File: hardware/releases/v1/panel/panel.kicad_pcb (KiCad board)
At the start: 4 copper layers, 126 x 56 mm, 125 parts, among them J1 12-32V DC In, J101 Main board, J102 XD_NORTH, J103 XD_EAST, J104 XD_SOUTH, J105 XD_WEST, J106 PIEZO_RAIN, J2 Crown board, J201 Probe T-Header SMD, J3 Probe board, J301 Main board, J302 Reflector T-Socket SMD, J4 SEN55 PM, Q1 AO3400A, Q301 AO3400A, SW1 SERVICE, U1 SCT2400TVBR, U101 SN74LVC2G04, U102 CD4052BM96, U103 TLV9062IDR, U104 LM393DR2G, U105 TLV9062IDR, U106 LTR-390UV-01, U107 VEML7700-TT, U108 LIS2MDLTR, U2 LM66100, U3 XIAO ESP32C6, U301 SCD41-D-R2, U302 SGP41-D-R4, U303 SHT45-AD1F-R2, U304 LM393DR2G, U4 BMP581, U5 LSM6DS3TR-C, U6 AS3935-BQFT, U7 74AHCT1G125

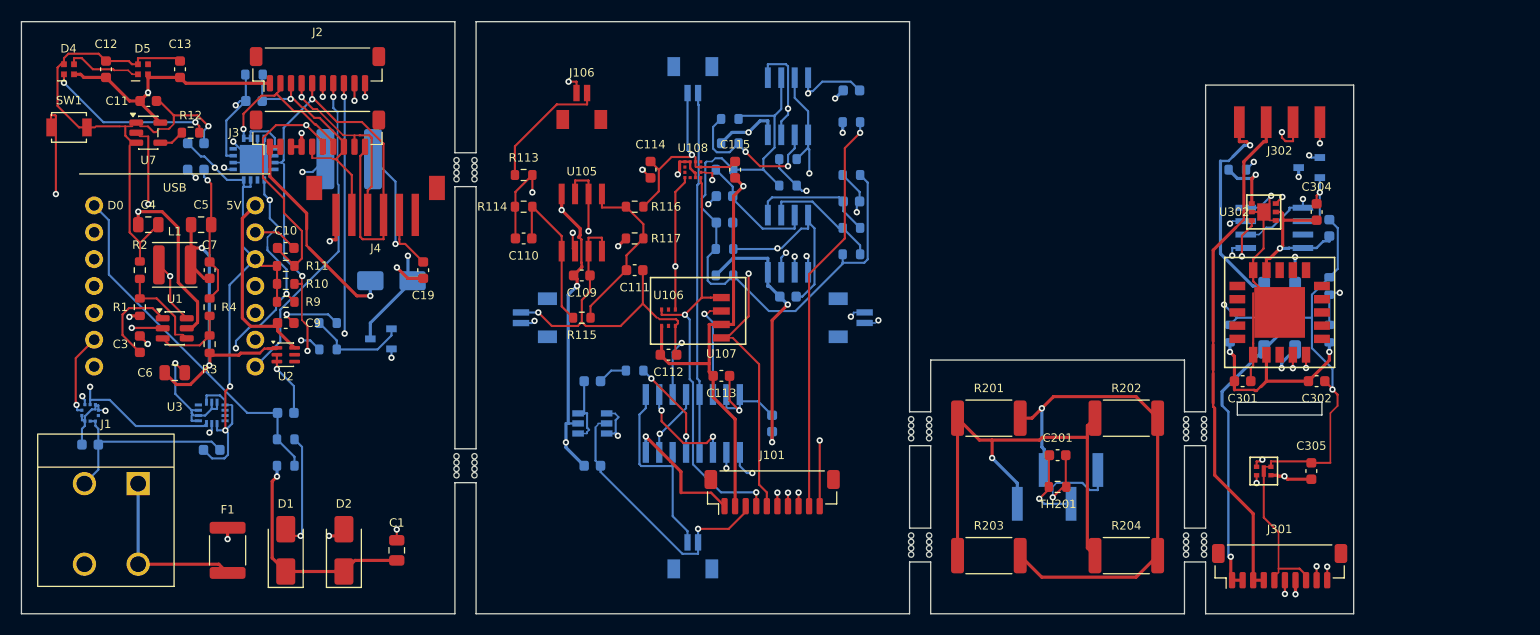
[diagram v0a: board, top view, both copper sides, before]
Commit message: Update project documentation and refactor crown sensor board circuit implementation
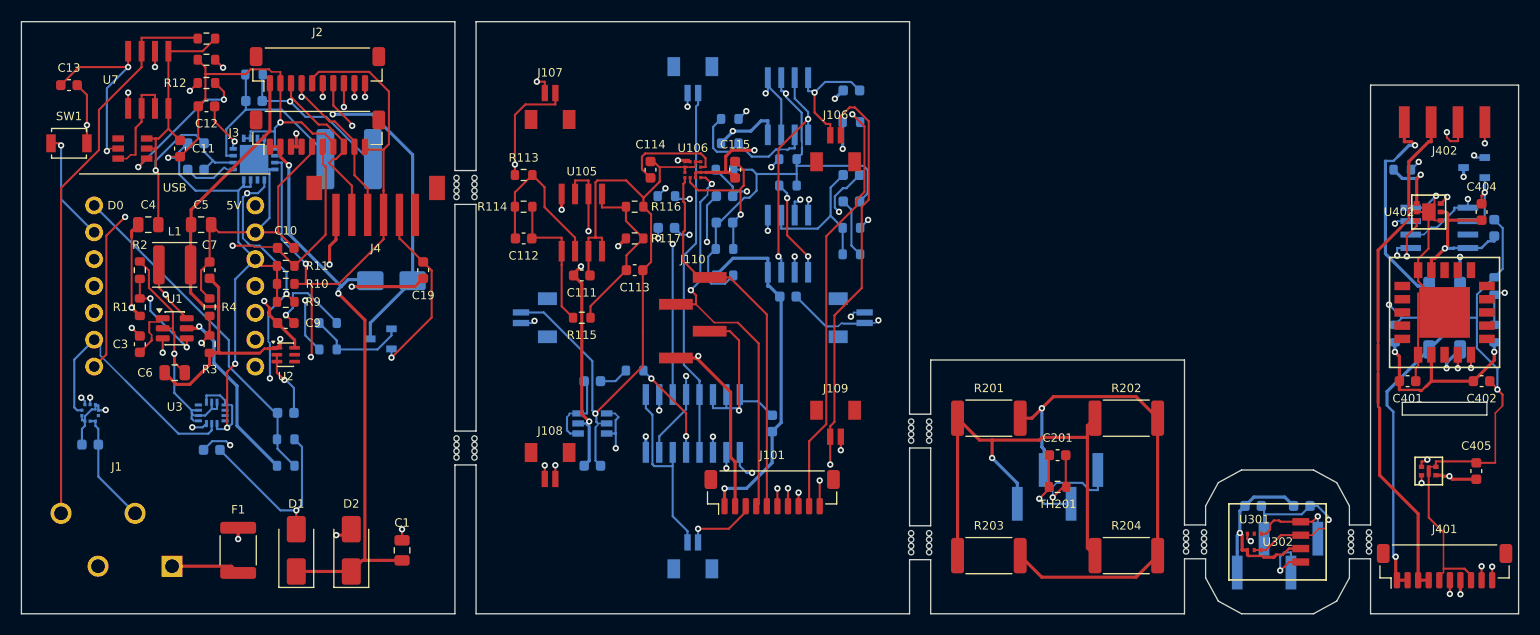
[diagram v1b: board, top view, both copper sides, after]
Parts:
- removed D4: RGB STATUS, gateway_fp:LED_SK6805-EC15_1.5x1.5mm
- removed D5: RGB WEATHER, gateway_fp:LED_SK6805-EC15_1.5x1.5mm
- removed U107: VEML7700-TT, gateway_fp:Vishay_VEML7700-TT
- removed U108: LIS2MDLTR, gateway_fp:ST_LIS2MDLTR_LGA-12
- added C301: 100n 50V, Capacitor_SMD:C_0603_1608Metric, B.Cu at (116.5, -10.2)
- added C302: 100n 50V, Capacitor_SMD:C_0603_1608Metric, B.Cu at (121.1, -10.2)
- added J107: PIEZO_NW, gateway_fp:JST_BM02B-SRSS-TB, F.Cu at (50.0, -48.0)
- added J108: PIEZO_SW, gateway_fp:JST_BM02B-SRSS-TB, F.Cu at (50.0, -14.0)
- added J109: PIEZO_SE, gateway_fp:JST_BM02B-SRSS-TB, F.Cu at (77.0, -18.0)
- added J110: DOME_RISER, gateway_fp:HX_PZ2.54-1x4P-SMD, F.Cu at (63.5, -28.0)
- added J301: CROWN_RISER, gateway_fp:HX_PZ2.54-1x4P-SMD, B.Cu at (118.8, -5.50)
- added R14: 4k7, Resistor_SMD:R_0603_1608Metric, F.Cu at (17.5, -54.4)
- added R15: 10k, Resistor_SMD:R_0603_1608Metric, B.Cu at (22.0, -51.0)
- added U301: LTR-390UV-01, gateway_fp:LiteOn_LTR-390UV-01, F.Cu at (116.6, -6.80)
- added U302: VEML7700-TT, gateway_fp:Vishay_VEML7700-TT, F.Cu at (121.0, -6.80)
- added U8: SN74LVC2G04DBVR, gateway_fp:TI_SN74LVC2G04_SOT-23-6, F.Cu at (10.5, -44.0)
- C105: value 47n 50V -> 100n 50V
- C106: value 100n 50V -> 47n 50V
- C108, C112: value 100n 50V -> 18p C0G 50V
- C109: value 100n 50V -> 47n 50V; moved to B.Cu
- C110: value 47n 50V -> 100n 50V; moved to B.Cu
- C111: value 220n 50V -> 100n 50V
- C113: value 100n 50V -> 220n 50V
- J1: value 12-32V DC In -> 12-32V + RS485; footprint gateway_fp:TerminalBlock_Kefa_KF142R-5.08-2P -> gateway_fp:TerminalBlock_Kefa_KF250-3.5-4P
- J102: value XD_NORTH -> XD_North
- J103: value XD_EAST -> XD_East
- J104: value XD_SOUTH -> XD_South
- J105: value XD_WEST -> XD_West
- J106: value PIEZO_RAIN -> PIEZO_NE
- R12: value 330R -> 1k
- R13: value 10k -> 4k7; moved to F.Cu
- U101: value SN74LVC2G04 -> SN74LVC2G04DBVR
- U106: value LTR-390UV-01 -> LIS2MDLTR; footprint gateway_fp:LiteOn_LTR-390UV-01 -> gateway_fp:ST_LIS2MDLTR_LGA-12
- U7: value 74AHCT1G125 -> SP3485EN-L/TR; footprint Package_TO_SOT_SMD:SOT-23-5 -> gateway_fp:ON_LM393DR2G_SOIC-8
- moved C110 34.0 mm to (78.5, -49.5)
- moved J106 24.3 mm to (77.0, -44.0)
- moved C112 17.6 mm to (47.5, -35.5)
- moved C403 15.6 mm to (139.3, -36.5)
- moved Q401 15.6 mm to (137.4, -42.2)
- moved R403 15.6 mm to (129.9, -26.5)
- moved R404 15.6 mm to (139.3, -26.5)
- moved R405 15.6 mm to (139.3, -31.0)
- moved C401 15.6 mm to (131.1, -22.0)
- moved C402 15.6 mm to (138.1, -22.0)
- moved C404 15.6 mm to (138.1, -38.0)
- moved C405 15.6 mm to (137.6, -13.5)
- moved J401 15.6 mm to (134.6, -4.50)
- moved J402 15.6 mm to (134.6, -46.5)
- moved R401 15.6 mm to (134.6, -25.0)
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- renumbered C301 to C401, C302 to C402, C303 to C403, C304 to C404, C305 to C405, J301 to J401, J302 to J402, Q301 to Q401, R301 to R401, R302 to R402, R303 to R403, R304 to R404, R305 to R405, R306 to R406, TH301 to TH401, U301 to U401, U302 to U402, U303 to U403, U304 to U404
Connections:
- C105 pad 1: CROWN_US_RX_MUX -> CROWN_+5V
- C105 pad 2: CROWN_US_AMP1_IN -> CROWN_GND
- C106 pad 1: CROWN_+5V -> CROWN_US_RX_MUX
- C106 pad 2: CROWN_GND -> CROWN_US_AMP1_IN
- C107 pad 1: CROWN_US_AMP1_OUT -> CROWN_N$2
- C107 pad 2: CROWN_US_AMP2_IN -> CROWN_US_VREF
- C108 pad 1: CROWN_+5V -> CROWN_US_AMP1_FB
- C108 pad 2: CROWN_GND -> CROWN_US_AMP1_OUT
- C109 pad 1: CROWN_+5V -> CROWN_US_AMP1_OUT
- C109 pad 2: CROWN_GND -> CROWN_US_AMP2_IN
- C11 pad 1: +5V -> +3V3
- C110 pad 1: CROWN_PIEZO_INV -> CROWN_+5V
- C110 pad 2: CROWN_PIEZO_STG1 -> CROWN_GND
- C111 pad 1: CROWN_PIEZO_ENV -> CROWN_+5V
- C112 pad 1: CROWN_+3V3 -> CROWN_PIEZO_INV
- C112 pad 2: CROWN_GND -> CROWN_PIEZO_STG1
- C113 pad 1: CROWN_+3V3 -> CROWN_PIEZO_ENV
- C12 pad 1: +5V -> +3V3
- C13 pad 1: +5V -> +3V3
- R105 pad 1: CROWN_US_VREF -> CROWN_US_AMP1_FB
- R105 pad 2: CROWN_US_AMP1_FB -> CROWN_N$2
- R108 pad 1: CROWN_US_VREF -> CROWN_US_AMP2_FB
- R108 pad 2: CROWN_US_AMP2_FB -> CROWN_US_VREF
- R12 pad 1: N$1 -> RS485_RO
- R12 pad 2: N$2 -> RS485_IO
- R13 pad 1: AS_INP -> +3V3
- R13 pad 2: GND -> RS485_A
- U106 pad 1: CROWN_+3V3 -> CROWN_I2C_SCL
- U106 pad 2: (no net) -> CROWN_GND
- U106 pad 3: CROWN_GND -> CROWN_+3V3
- U106 pad 4: CROWN_I2C_SCL -> CROWN_I2C_SDA
- U106 pad 5: (no net) -> CROWN_+3V3
- U106 pad 6: CROWN_I2C_SDA -> CROWN_LIS_C1
- U3 pad 11: LED_DATA -> RS485_IO
- U7 pad 1: GND -> RS485_RO
- U7 pad 2: LED_DATA -> RS485_DE
- U7 pad 3: GND -> RS485_DE
- U7 pad 4: N$1 -> GND
- U7 pad 5: +5V -> GND
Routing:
- net CROWN_PIEZO_IN: track 12.3 -> 112.1 mm, vias 0 -> 3
- net RS485_A: track 0.00 -> 62.0 mm, vias 0 -> 2
- net RS485_B: track 0.00 -> 53.5 mm
- net NTC_SENSE: track 82.8 -> 43.5 mm
- net +3V3: track 96.5 -> 135.7 mm, vias 5 -> 8
- net RS485_IO: track 0.00 -> 32.7 mm, vias 0 -> 2
- net GND: track 168.6 -> 199.2 mm, vias 13 -> 11
- net +5V: track 99.0 -> 71.0 mm, vias 5 -> 3
- net CROWN_US_AMP1_OUT: track 11.9 -> 37.0 mm, vias 0 -> 4
- net LED_DATA: track 21.0 -> 0.00 mm, vias 1 -> 0
- net DOME_+3V3: track 0.00 -> 20.0 mm, vias 0 -> 1
- net DOME_GND: track 0.00 -> 17.9 mm, vias 0 -> 1
- net N$2: track 15.9 -> 0.00 mm, vias 2 -> 0
- net CROWN_RAIN_ADC: track 60.3 -> 44.6 mm
- net US_RX: track 41.8 -> 27.7 mm
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- added copper zone on In1.Cu, net DOME_GND
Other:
- board size 126 x 56 mm -> 141.6 x 56 mm

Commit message: Update documentation to reflect hardware specification changes and component substitutions
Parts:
- removed C115: 100n 50V, Capacitor_SMD:C_0603_1608Metric
- C114: value 220n 50V -> 100n 50V
- J110: value DOME_RISER -> DOME_SOCKET
- U106: value LIS2MDLTR -> MMC5603NJ; footprint gateway_fp:ST_LIS2MDLTR_LGA-12 -> gateway_fp:MEMSIC_MMC5603NJ_WLCSP-4
- U403: value SHT45-AD1F-R2 -> SHT40-AD1F-R2
- moved C302 8.42 mm to (118.8, -2.10)
- moved C114 7.50 mm to (67.0, -42.0)
- moved C301 2.64 mm to (118.8, -11.5)
- moved J301 1.30 mm to (118.8, -6.80)
- turned J110 to 0 degrees
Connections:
- C114 pad 1: CROWN_LIS_C1 -> CROWN_+3V3
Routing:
- net CROWN_GND: track 134.9 -> 113.5 mm, vias 11 -> 13
- net CROWN_+3V3: track 72.0 -> 60.6 mm, vias 5 -> 3
- net CROWN_LIS_C1: track 9.97 -> 0.00 mm
- net CROWN_XD_E: track 27.7 -> 36.2 mm
- net CROWN_RAIN_ADC: track 44.6 -> 51.6 mm
- net CROWN_US_VREF: track 48.4 -> 55.2 mm, vias 2 -> 3
- net CROWN_I2C_SDA: track 38.6 -> 34.3 mm, vias 2 -> 0
- net CROWN_US_AMP2_OUT: track 33.9 -> 38.0 mm
- net CROWN_US_AMP1_OUT: track 37.0 -> 32.8 mm, vias 4 -> 2
- net CROWN_+5V: track 116.5 -> 120.4 mm, vias 7 -> 9
- net CROWN_PIEZO_ENV: track 16.8 -> 19.4 mm
- net DOME_I2C_SCL: track 8.54 -> 11.1 mm
- net CROWN_US_AMP2_FB: track 24.3 -> 26.8 mm
- net DOME_I2C_SDA: track 11.5 -> 13.3 mm, vias 2 -> 1
- net DOME_GND: track 17.9 -> 16.3 mm
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
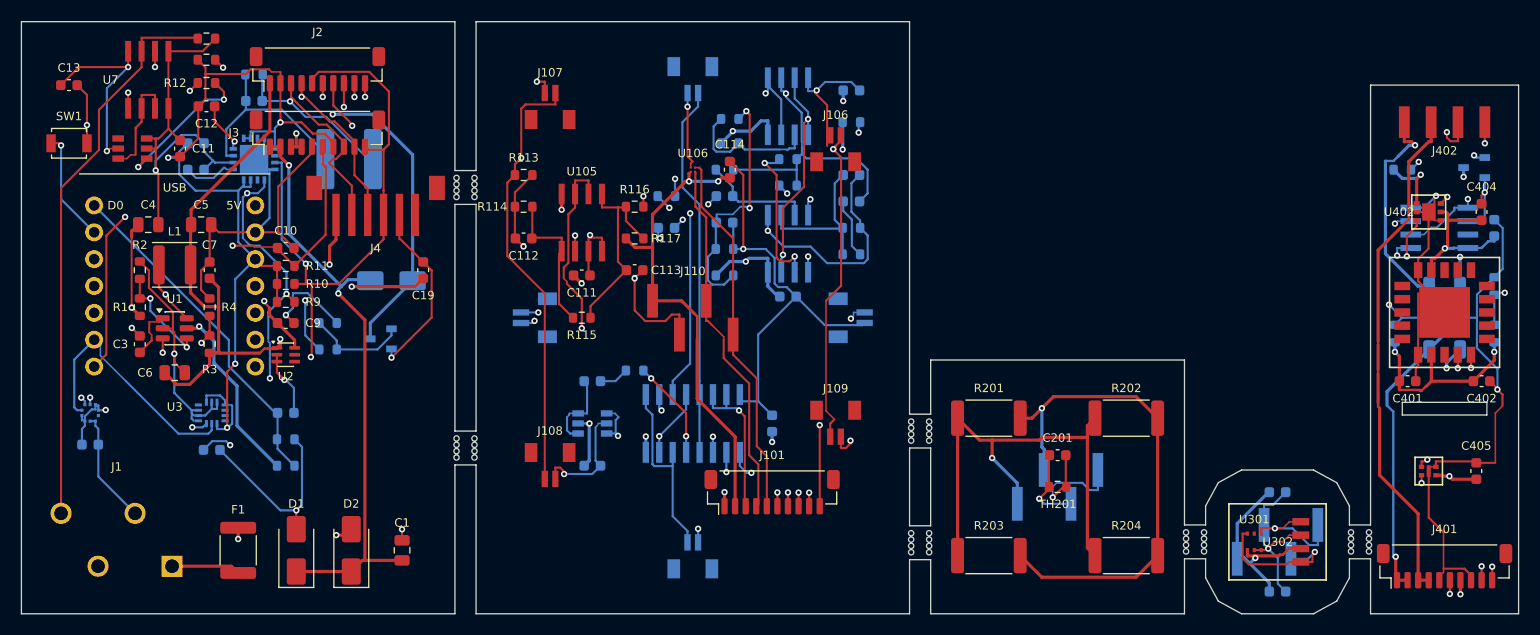
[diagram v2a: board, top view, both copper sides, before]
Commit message: Redesign crown PCB
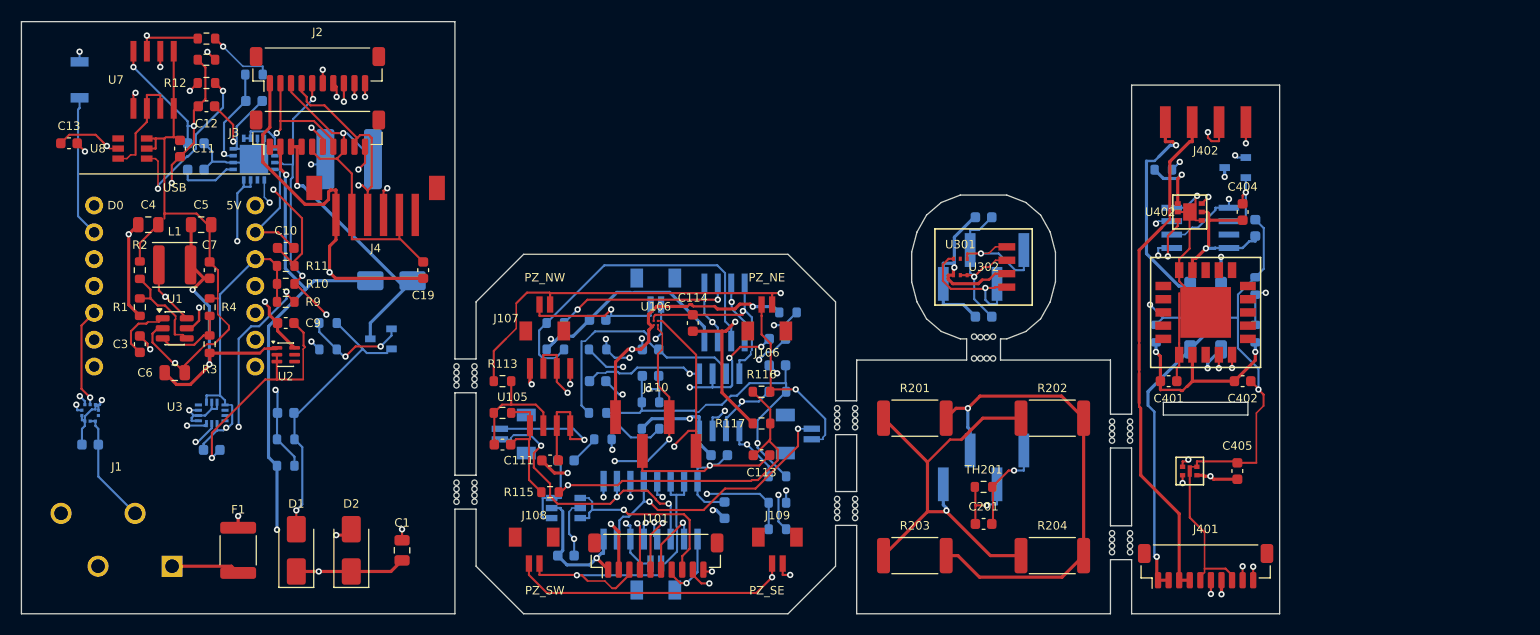
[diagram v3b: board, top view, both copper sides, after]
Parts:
- SW1: moved to B.Cu
- moved C301 38.1 mm to (91.0, -37.5)
- moved C302 38.1 mm to (91.0, -28.1)
- moved J301 38.1 mm to (91.0, -32.8)
- moved U301 38.1 mm to (88.8, -32.8)
- moved U302 38.1 mm to (93.2, -32.8)
- moved C110 32.4 mm to (54.5, -27.8)
- moved R107 27.5 mm to (71.5, -13.0)
- moved R105 26.9 mm to (71.5, -8.00)
- moved R106 26.9 mm to (71.5, -10.5)
- moved R104 25.9 mm to (54.5, -19.0)
- moved R110 25.5 mm to (50.5, -25.0)
- moved R111 25.4 mm to (50.5, -27.5)
- moved C403 22.6 mm to (116.7, -36.5)
- moved Q401 22.6 mm to (114.8, -42.2)
- moved R403 22.6 mm to (107.3, -26.5)
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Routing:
- net NTC_SENSE: track 43.5 -> 74.7 mm
- net CROWN_PIEZO_ENV: track 19.4 -> 43.5 mm, vias 0 -> 2
- net CROWN_+5V: track 120.4 -> 100.0 mm, vias 9 -> 6
- net US_TX: track 28.8 -> 48.2 mm
- net CROWN_US_VTH: track 12.9 -> 32.2 mm
- net CROWN_US_VREF: track 55.2 -> 73.6 mm
- net CROWN_PIEZO_IN: track 111.5 -> 93.7 mm
- net CROWN_GND: track 113.5 -> 130.9 mm, vias 13 -> 9
- net CROWN_US_AMP1_FB: track 15.2 -> 32.0 mm, vias 0 -> 4
- net I2C_SCL: track 102.5 -> 86.9 mm, vias 2 -> 7
- net CROWN_RAIN_ADC: track 51.6 -> 37.0 mm
- net CROWN_US_AMP1_IN: track 10.5 -> 23.4 mm
- net CROWN_N$2: track 5.66 -> 18.1 mm, vias 0 -> 2
- net GND: track 199.2 -> 187.9 mm
- net CROWN_XD_N: track 35.3 -> 25.1 mm, vias 0 -> 3
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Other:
- board size 141.6 x 56 mm -> 119 x 56 mm
- board text added: "PZ_NE"
- board text added: "PZ_NW"
- board text added: "PZ_SE"
- board text added: "PZ_SW"
- board text added: "US_E"
- board text added: "US_N"
- board text added: "US_S"
- board text added: "US_W"

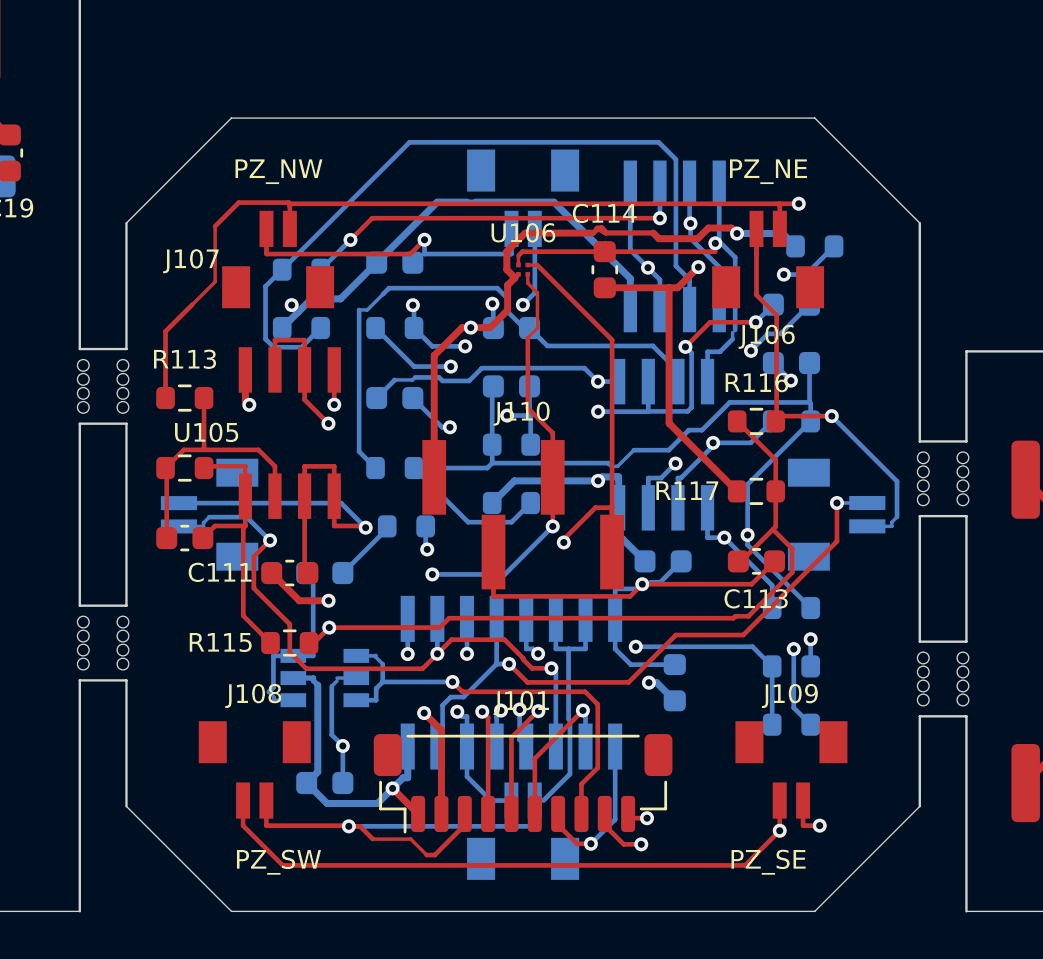
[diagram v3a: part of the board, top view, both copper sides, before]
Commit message: Move all 10 connectors to top layer and reorganize component placement for improved assembly
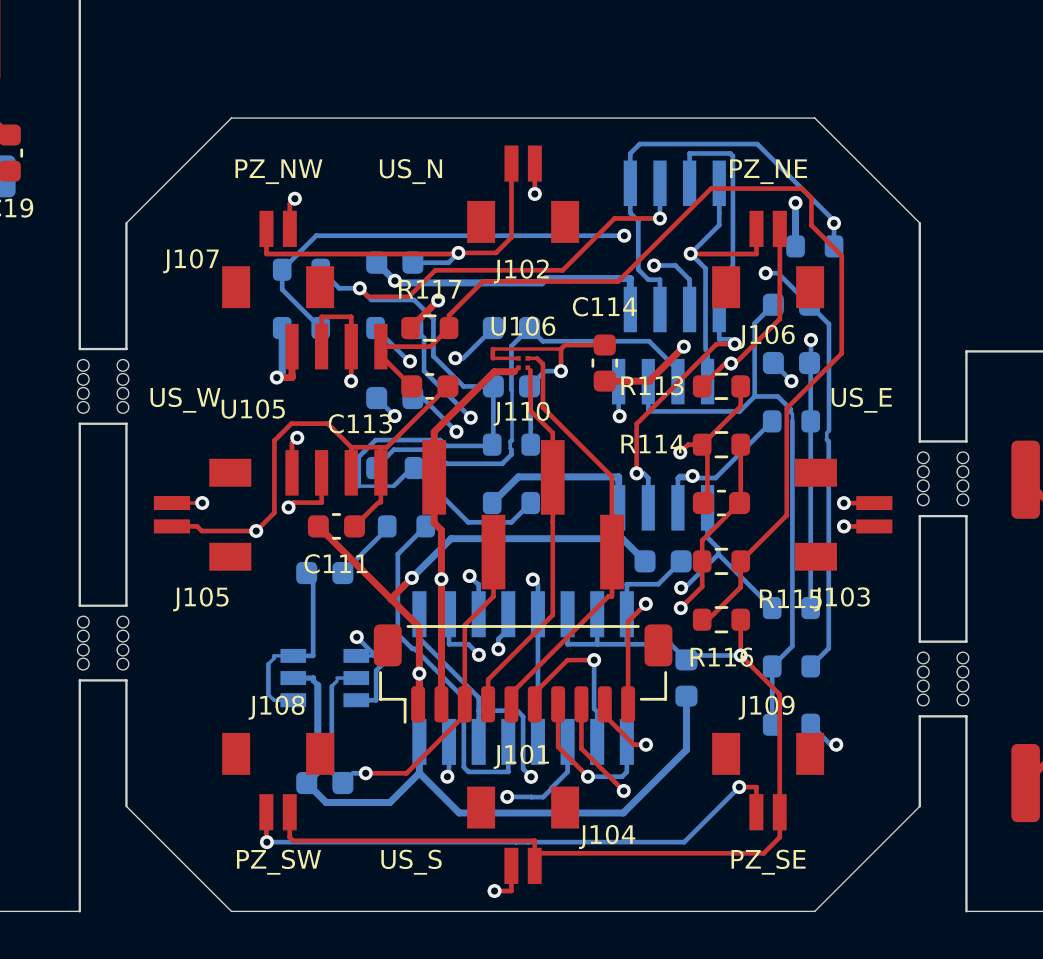
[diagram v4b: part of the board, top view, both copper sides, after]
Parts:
- J102, J103, J104, J105: moved to F.Cu
- moved C112 23.0 mm to (68.5, -17.5)
- moved R114 23.0 mm to (68.5, -20.0)
- moved R113 23.0 mm to (68.5, -22.5)
- moved R115 18.8 mm to (68.5, -15.0)
- moved C113 15.9 mm to (56.0, -22.5)
- moved R117 15.7 mm to (56.0, -25.0)
- moved R116 8.63 mm to (68.5, -12.5)
- moved J101 4.70 mm to (60.0, -10.2)
- moved C114 4.00 mm to (63.5, -23.5)
- moved U106 4.00 mm to (60.0, -23.5)
- moved C111 2.83 mm to (52.0, -16.5)
- moved U105 2.24 mm to (52.0, -21.5)
- moved J108 1.12 mm to (49.5, -5.50)
- moved J109 1.12 mm to (70.5, -5.50)
- moved C103 0.54 mm to (67.0, -10.0)
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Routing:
- net CROWN_PIEZO_INV: track 11.8 -> 37.4 mm, vias 0 -> 2
- net CROWN_PIEZO_STG1: track 11.9 -> 30.9 mm, vias 0 -> 2
- net CROWN_XD_E: track 27.2 -> 41.5 mm, vias 2 -> 3
- net CROWN_I2C_SCL: track 31.3 -> 18.4 mm, vias 2 -> 0
- net CROWN_I2C_SDA: track 28.9 -> 16.0 mm, vias 3 -> 0
- net CROWN_US_AMP2_IN: track 33.7 -> 22.5 mm
- net CROWN_XD_N: track 25.1 -> 34.9 mm, vias 3 -> 2
- net CROWN_US_VTH: track 32.2 -> 23.3 mm, vias 0 -> 2
- net CROWN_US_TX: track 18.4 -> 26.9 mm, vias 1 -> 2
- net CROWN_XD_S: track 10.3 -> 18.6 mm
- net CROWN_PIEZO_IN: track 93.7 -> 85.6 mm, vias 2 -> 4
- net CROWN_+3V3: track 65.9 -> 57.9 mm
- net CROWN_XD_W: track 27.8 -> 35.7 mm
- net CROWN_US_AMP2_OUT: track 41.2 -> 34.6 mm, vias 4 -> 3
- net CROWN_RAIN_ADC: track 37.0 -> 30.4 mm
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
